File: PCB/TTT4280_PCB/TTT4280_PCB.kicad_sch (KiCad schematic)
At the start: 20 parts, among them J1 Raspberry Pi 3B+ Header, U1 MCP3201-CI/P, U2 MCP3201-CI/P, U3 MCP3201-CI/P, U4 MCP3201-CI/P, U5 MCP3201-CI/P

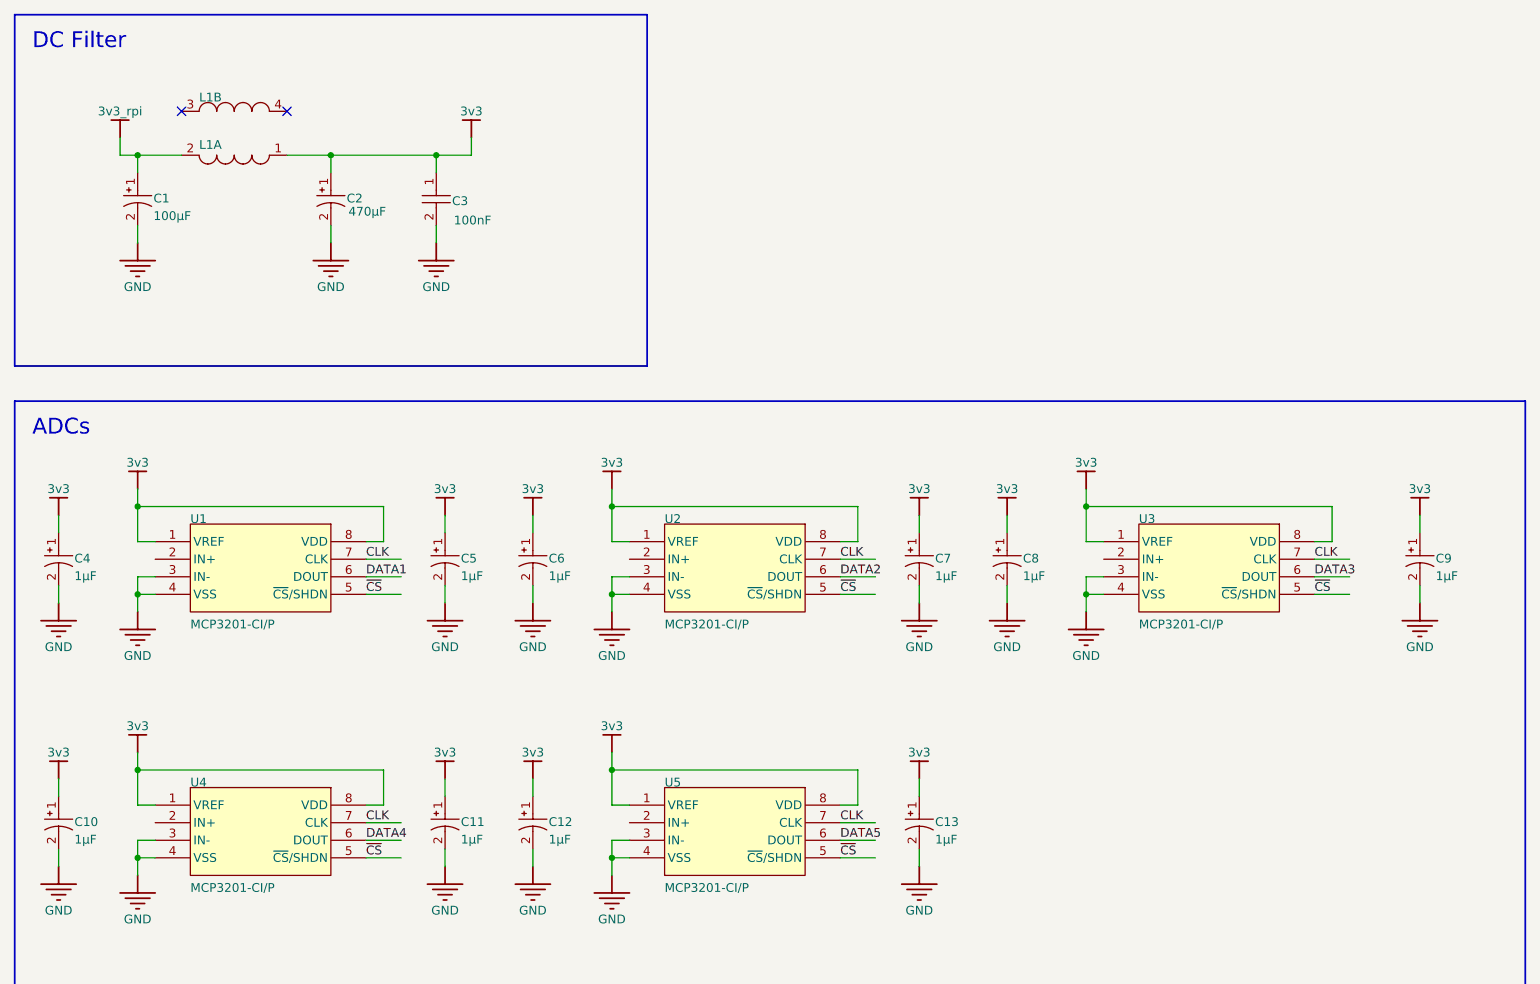
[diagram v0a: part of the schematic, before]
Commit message: Added microphones
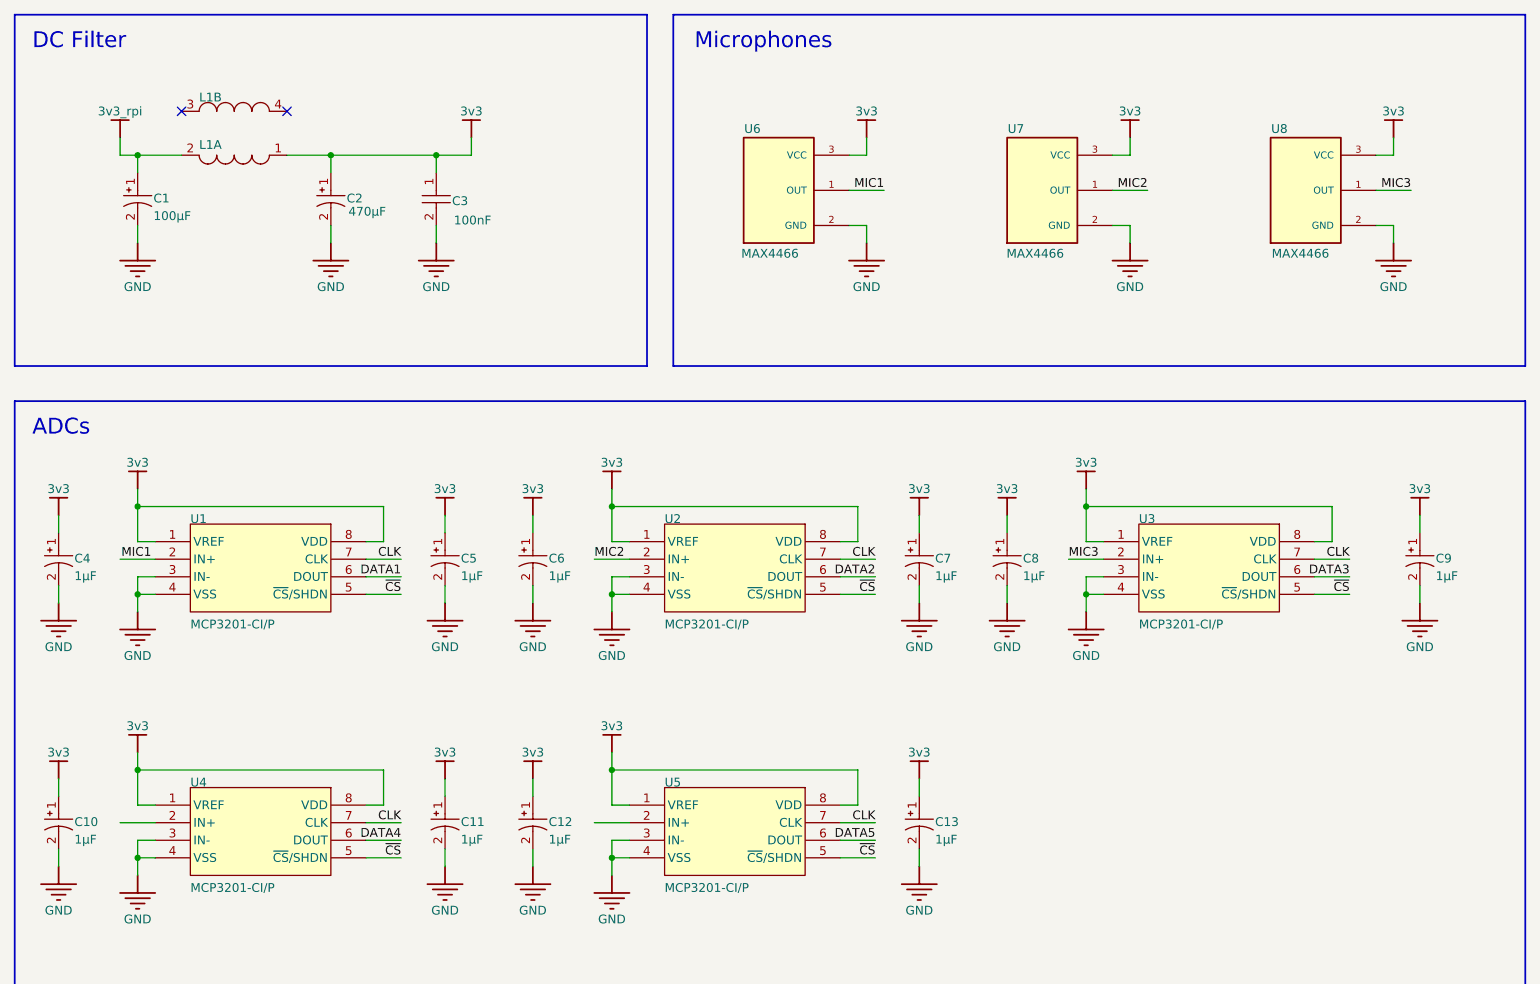
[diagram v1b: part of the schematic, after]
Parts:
- added U6, U7, U8: MAX4466, 1063:MODULE_1063, symbol max4466:1063
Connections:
- net 3v3: now also U6.3 (VCC), U7.3 (VCC), U8.3 (VCC)
- net GND: now also U6.2 (GND), U7.2 (GND), U8.2 (GND)
- net MIC1: now reaches U1.2 (IN+)
- net MIC1: now also U6.1 (OUT)
- net MIC3: now reaches U3.2 (IN+)
- net MIC3: now also U8.1 (OUT)
- net MIC2: now reaches U2.2 (IN+)
- net MIC2: now also U7.1 (OUT)
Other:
- note added: "Microphones"

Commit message: Made updates to PCB, schematic done.
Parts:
- removed C1: ECA1EM101, CAPPR55-250-1120X630X1220, symbol Main-altium-import:root_0_CAP-P-2_sindrekvam
- removed C10, C11, C12, C13, C4, C5, C6, C7, C8, C9: 7110918, CAPPR55-200-1100X500X1200, symbol Main-altium-import:root_0_CAP-P-2_sindrekvam
- removed C2: ECA1CM471, CAPPR65-350-1150X800X1250, symbol Main-altium-import:root_0_CAP-P-2_sindrekvam
- removed C3: C320C104K1R5TA, C320C104K1R5TA, symbol Main-altium-import:root_3_CAP-NP-2_sindrekvam
- removed J1: Raspberry Pi 3B+ Header, HDRV40W85P254_2X20_5080X500X860P, symbol Main-altium-import:root_0_Raspberry Pi 3B+ header_sindrekvam
- removed L1: DKFP-G22G-D5J0, DKFPG22GD5J0, symbol Main-altium-import:root_0_Dual inductor_sindrekvam
- removed U1, U2, U3, U4, U5: MCP3201-CI/P, MCHP-P-8, symbol Main-altium-import:root_0_MCP3201_sindrekvam
- removed U6, U7, U8: MAX4466, 1063:MODULE_1063, symbol max4466:1063
- added C1, C10, C11, C12, C13, C2, C6, C7, C8, C9: 1uF, Capacitor_SMD:C_0603_1608Metric_Pad1.08x0.95mm_HandSolder, symbol Device:C_Polarized
- added C14, C15: 1nF, Capacitor_SMD:C_0603_1608Metric_Pad1.08x0.95mm_HandSolder, symbol Device:C
- added C16, C17: 45.5uF, Capacitor_SMD:C_0603_1608Metric_Pad1.08x0.95mm_HandSolder, symbol Device:C
- added C18, C21, C5: 100nF, Capacitor_SMD:C_0603_1608Metric_Pad1.08x0.95mm_HandSolder, symbol Device:C
- added C19, C20: 5.7nF, Capacitor_SMD:C_0603_1608Metric_Pad1.08x0.95mm_HandSolder, symbol Device:C
- added C3, C4: 100uF, Capacitor_SMD:C_0603_1608Metric_Pad1.08x0.95mm_HandSolder, symbol Device:C_Polarized
- added J1: Raspberry_Pi_2_3, Connector_PinHeader_2.54mm:PinHeader_2x20_P2.54mm_Vertical, symbol Connector:Raspberry_Pi_2_3
- added J2: Conn_01x02_Pin, Connector_PinHeader_2.54mm:PinHeader_1x02_P2.54mm_Vertical, symbol Connector:Conn_01x02_Pin
- added L1: L_Iron_Coupled_1423, symbol Device:L_Iron_Coupled_1423
- added R1, R2, R3, R4: 1k, Resistor_SMD:R_0603_1608Metric_Pad0.98x0.95mm_HandSolder, symbol Device:R
- added R5, R6, R7, R8: 10k, Resistor_SMD:R_0603_1608Metric_Pad0.98x0.95mm_HandSolder, symbol Device:R
- added U1, U2, U3, U4, U8: MCP3201, Package_DIP:DIP-8_W7.62mm, symbol Analog_ADC:MCP3201
- added U10: MCP6002-xMC, Package_DIP:DIP-8_W7.62mm, symbol Amplifier_Operational:MCP6002-xMC
- added U5: K-LC6, Connector_PinSocket_2.54mm:PinSocket_1x05_P2.54mm_Horizontal, symbol RF:K-LC6
- added U6, U7, U9: MAX4466, Connector_PinHeader_2.54mm:PinHeader_1x03_P2.54mm_Vertical, symbol Sensor_Audio:MAX4466
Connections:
- net CLK: now also J1.23 (SCLK0/GPIO11), U1.7 (CLK), U2.7 (CLK), U3.7 (CLK), U4.7 (CLK), U8.7 (CLK)
- net DATA1: now also J1.16 (GPIO23), U1.6 (Dout)
- net DATA2: now also J1.18 (GPIO24), U3.6 (Dout)
- net DATA3: now also J1.22 (GPIO25), U8.6 (Dout)
- net DATA4: now also J1.37 (GPIO26), U2.6 (Dout)
- net DATA5: now also J1.13 (GPIO27), U4.6 (Dout)
- net GND: now also C1.2, C10.2, C11.2, C12.2, C13.2, C14.2, C15.2, C18.1, C2.2, C21.1, C3.2, C4.2, C5.1, C6.2, C7.2, C8.2, C9.2, J1.14 (GND), J1.20 (GND), J1.25 (GND), J1.30 (GND), J1.34 (GND), J1.39 (GND), J1.6 (GND), J1.9 (GND), J2.2 (Pin_2), R1.2, R2.2, R8.1, U1.3 (IN-), U1.4 (Vss), U10.4 (V-), U10.9 (V-), U2.3 (IN-), U2.4 (Vss), U3.3 (IN-), U3.4 (Vss), U4.3 (IN-), U4.4 (Vss), U5.4 (GND), U6.2 (GND), U7.2 (GND), U8.3 (IN-), U8.4 (Vss), U9.2 (GND)
- net MIC1: now also U1.2 (IN+), U6.1 (OUT)
- net MIC2: now also U3.2 (IN+), U7.1 (OUT)
- net MIC3: now also U8.2 (IN+), U9.1 (OUT)
- net ~{CS}: now also J1.24 (~{CE0}/GPIO8), U1.5 (~{CS}/SHDN), U2.5 (~{CS}/SHDN), U3.5 (~{CS}/SHDN), U4.5 (~{CS}/SHDN), U8.5 (~{CS}/SHDN)
- new net: C16.2, R3.1
- new net: C19.1, R3.2, R5.1, U10.2 (-)
- new net: C20.1, R4.2, R6.1, U10.6 (-)
- new net: C17.2, R4.1
- new net: J1.2 (5V), J1.4 (5V)
- new net +1V65: C21.2, R7.1, R8.2, U10.3 (+), U10.5 (+)
- new net +3V3: C1.1, C10.1, C11.1, C12.1, C13.1, C18.2, C2.1, C3.1, C4.1, C5.2, C6.1, C7.1, C8.1, C9.1, J1.1 (3V3), J1.17 (3V3), L1.1, L1.4, R7.2, U1.1 (Vref), U1.8 (Vdd), U10.8 (V+), U2.1 (Vref), U2.8 (Vdd), U3.1 (Vref), U3.8 (Vdd), U4.1 (Vref), U4.8 (Vdd), U6.3 (VCC), U7.3 (VCC), U8.1 (Vref), U8.8 (Vdd), U9.3 (VCC)
- new net +5V: J2.1 (Pin_1), U5.2 (VCC)
- new net IF_I: C14.1, C16.1, R1.1, U5.3 (IF_I)
- new net IF_Q: C15.1, C17.1, R2.1, U5.1 (IF_Q)
- new net filtered_I: C19.2, R5.2, U10.1, U2.2 (IN+)
- new net filtered_Q: C20.2, R6.2, U10.7, U4.2 (IN+)
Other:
- note added: "Power header"
- note added: "Radar active filters"
- note added: "Radar header"
